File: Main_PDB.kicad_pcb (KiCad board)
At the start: 4 copper layers, 175.5 x 85.5 mm, 134 parts, among them Q4 NMOS, Q5 NMOS, Q6 NMOS, Q7 NMOS, Q8 NMOS, U10 ACS758LCB-100U-PFF-T, U11 ACS758LCB-100U-PFF-T, U12 ACS758LCB-100U-PFF-T, U2 LM5148RGYR, U3 LMR36015ARNXR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

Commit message: fixed grounding error
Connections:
- CBLK3 pad 2: AGND -> PGND
- CBLK4 pad 2: AGND -> PGND
- CBLK5 pad 2: AGND -> PGND
- CBLK6 pad 2: AGND -> PGND
- CBLK7 pad 2: AGND -> PGND
- CBLK8 pad 2: AGND -> PGND
- CBLKA1 pad 2: AGND -> PGND
- CBLKA2 pad 2: AGND -> PGND
- CBLKA3 pad 2: AGND -> PGND
- CBLKA4 pad 2: AGND -> PGND
- CBULK1 pad 2: AGND -> PGND
- CBULK2 pad 2: AGND -> PGND
- CHF4A1 pad 2: AGND -> PGND
- CIN1A1 pad 2: AGND -> PGND
- CIN1B1 pad 2: AGND -> PGND
- CIN1B2 pad 2: AGND -> PGND
- CIN2A1 pad 2: AGND -> PGND
- CIN2B1 pad 1: AGND -> PGND
- CIN2B2 pad 1: AGND -> PGND
- CIN3A1 pad 2: AGND -> PGND
- CIN3B1 pad 1: AGND -> PGND
- CIN3B2 pad 1: AGND -> PGND
- CIN4B1 pad 1: AGND -> PGND
- CIN4B2 pad 1: AGND -> PGND
- CIN5A1 pad 2: AGND -> PGND
- CIN5B1 pad 1: AGND -> PGND
- CIN5B2 pad 1: AGND -> PGND
- CINC1 pad 1: AGND -> PGND
- CINC10 pad 2: AGND -> PGND
- CINC11 pad 2: AGND -> PGND
- CINC12 pad 2: AGND -> PGND
- CINC2 pad 1: AGND -> PGND
- CINC3 pad 1: AGND -> PGND
- CINC4 pad 1: AGND -> PGND
- CINC5 pad 1: AGND -> PGND
- CINC6 pad 1: AGND -> PGND
- CINC7 pad 1: AGND -> PGND
- CINC8 pad 1: AGND -> PGND
- CINC9 pad 2: AGND -> PGND
- COUT1A1 pad 2: AGND -> PGND
- COUT1B1 pad 2: AGND -> PGND
- COUT1B2 pad 2: AGND -> PGND
- COUT2A1 pad 2: AGND -> PGND
- COUT2B1 pad 2: AGND -> PGND
- COUT2B2 pad 2: AGND -> PGND
- COUT3A1 pad 2: AGND -> PGND
- COUT3B1 pad 2: AGND -> PGND
- COUT3B2 pad 2: AGND -> PGND
- COUT4B1 pad 2: AGND -> PGND
- COUT4B2 pad 2: AGND -> PGND
- CVCC1 pad 2: AGND -> PGND
- CVCC2 pad 2: AGND -> PGND
- D1 pad 2: AGND -> PGND
- D2 pad 2: AGND -> PGND
- D3 pad 2: AGND -> PGND
- D4 pad 2: AGND -> PGND
- D5 pad 2: AGND -> PGND
- D6 pad 2: AGND -> PGND
- D7 pad 2: AGND -> PGND
- D8 pad 2: AGND -> PGND
- Q5 pad 3: AGND -> PGND
- Q6 pad 3: AGND -> PGND
- Q8 pad 3: AGND -> PGND
- RESTOP4 pad 2: AGND -> PGND
- RGND1 pad 1: AGND -> PGND
- U2 pad 10: AGND -> PGND
- U2 pad 25: AGND -> PGND
- U2 pad 7: unconnected-(U2-AGND-Pad7) -> AGND
- U3 pad 1: AGND -> PGND
- U3 pad 11: AGND -> PGND
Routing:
- net PGND: track 0.00 -> 9.73 mm, vias 0 -> 40
- net AGND: track 52.3 -> 42.6 mm, vias 41 -> 1
- added copper zone on B.Cu, net PGND
- added copper zone on F.Cu, net PGND
- added copper zone on In1.Cu, net PGND
- removed copper zone on B.Cu, net AGND
- removed copper zone on In1.Cu, net AGND

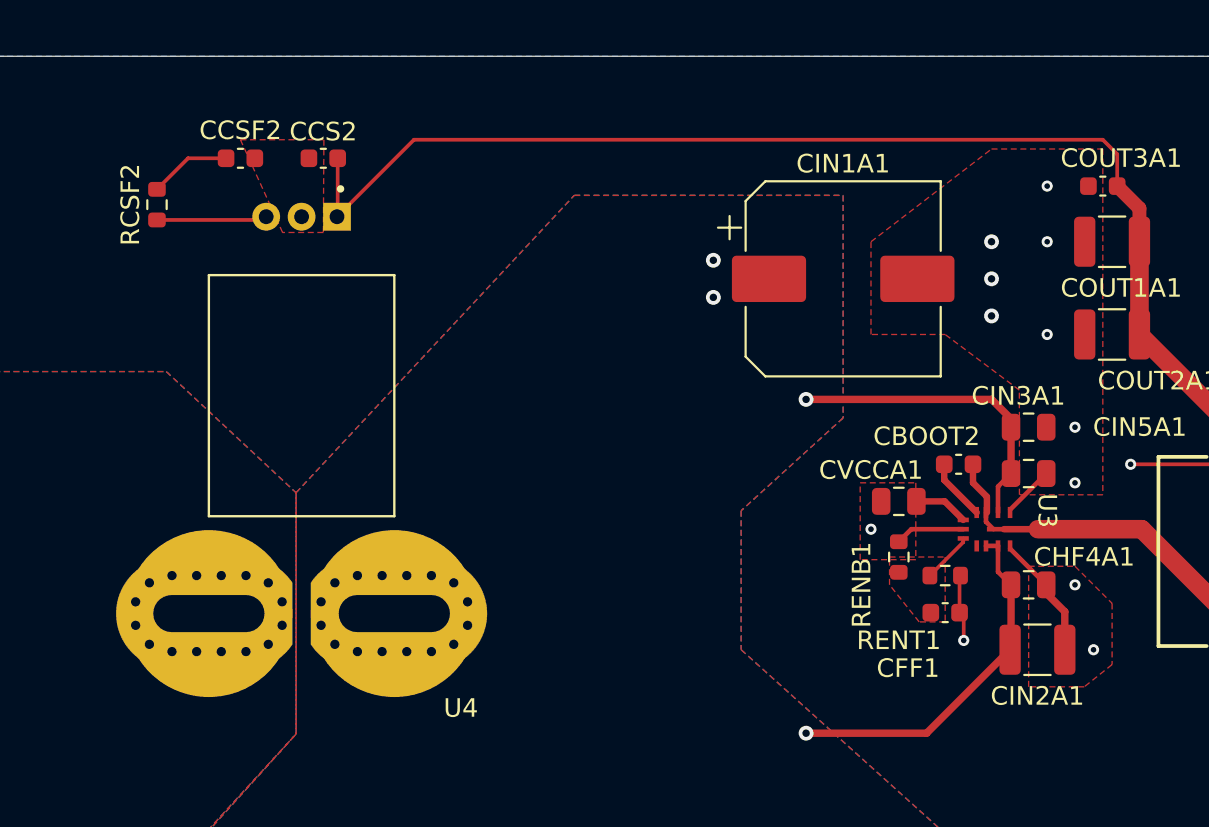
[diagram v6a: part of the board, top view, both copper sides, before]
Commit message: adj decoupling caps placements
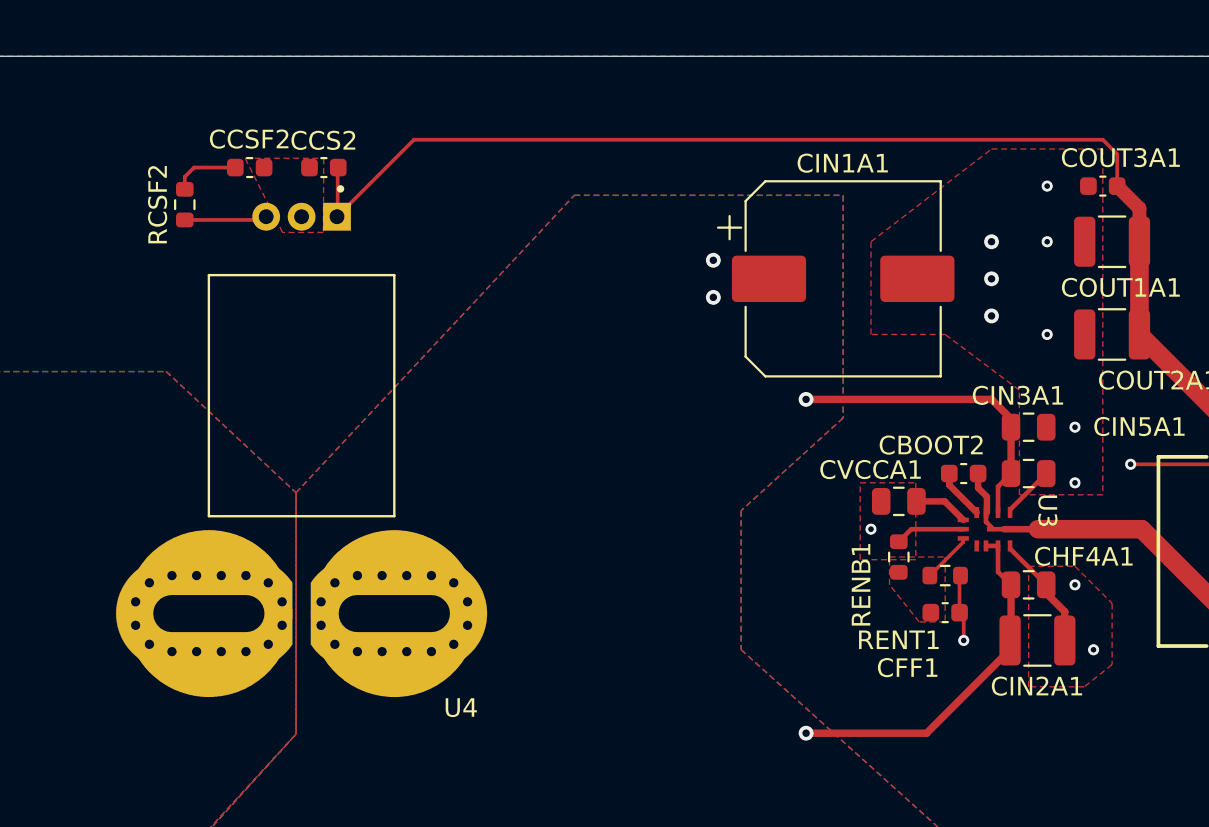
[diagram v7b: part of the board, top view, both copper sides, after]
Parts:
- moved RCSF2 1.50 mm to (445.5, 49.0)
- moved CCSF2 0.71 mm to (449.0, 47.0)
- moved CBOOT2 0.57 mm to (487.5, 63.5)
- moved CCS2 0.50 mm to (453.0, 47.0)
- moved CIN2A1 0.50 mm to (491.5, 72.5)
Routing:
- net Net-(U4-VIOUT): track 5.96 -> 4.46 mm
- net /Main_curr: track 4.42 -> 3.61 mm
- net Net-(U3-NC): track 21.2 -> 20.5 mm
